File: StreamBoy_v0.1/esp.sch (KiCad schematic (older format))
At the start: 1 part

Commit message: Bunch of stuff
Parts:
- added C? (x3): C, Capacitor_SMD:C_0805_2012Metric, symbol Device:C
- added R?: R, Resistor_SMD:R_0805_2012Metric, symbol Device:R
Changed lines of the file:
@@
+	1    0    0    -1
+$EndComp
+$Comp
+L Device:R R?
+U 1 1 5E0D3F66
+P 2500 3200
+AR Path="/5E0FF68C/5E0D3F66" Ref="R?"  Part="1"
+AR Path="/5E0FBAC6/5E0D3F66" Ref="R?"  Part="1"
+F 0 "R?" H 2570 3246 50  0000 L CNN
+F 1 "R" H 2570 3155 50  0000 L CNN
+F 2 "Resistor_SMD:R_0805_2012Metric" V 2430 3200 50  0001 C CNN
+F 3 "~" H 2500 3200 50  0001 C CNN
+	1    2500 3200
+	1    0    0    -1
+$EndComp
+$Comp
+L Device:C C?
+U 1 1 5E0D4C34
+P 2550 2400
+F 0 "C?" H 2665 2446 50  0000 L CNN
+F 1 "C" H 2665 2355 50  0000 L CNN
+F 2 "Capacitor_SMD:C_0805_2012Metric" H 2588 2250 50  0001 C CNN
+F 3 "~" H 2550 2400 50  0001 C CNN
+	1    2550 2400
+	1    0    0    -1
+$EndComp
+$Comp
+L Device:C C?
+U 1 1 5E0D4F10
+P 2550 2800
+F 0 "C?" H 2665 2846 50  0000 L CNN
+F 1 "C" H 2665 2755 50  0000 L CNN
+F 2 "Capacitor_SMD:C_0805_2012Metric" H 2588 2650 50  0001 C CNN
+F 3 "~" H 2550 2800 50  0001 C CNN
+	1    2550 2800
+	1    0    0    -1
+$EndComp
+$Comp
+L Device:C C?
+U 1 1 5E0D4F16
+P 2900 2800
+F 0 "C?" H 3015 2846 50  0000 L CNN
+F 1 "C" H 3015 2755 50  0000 L CNN
+F 2 "Capacitor_SMD:C_0805_2012Metric" H 2938 2650 50  0001 C CNN
+F 3 "~" H 2900 2800 50  0001 C CNN
+	1    2900 2800
 	1    0    0    -1
 $EndComp

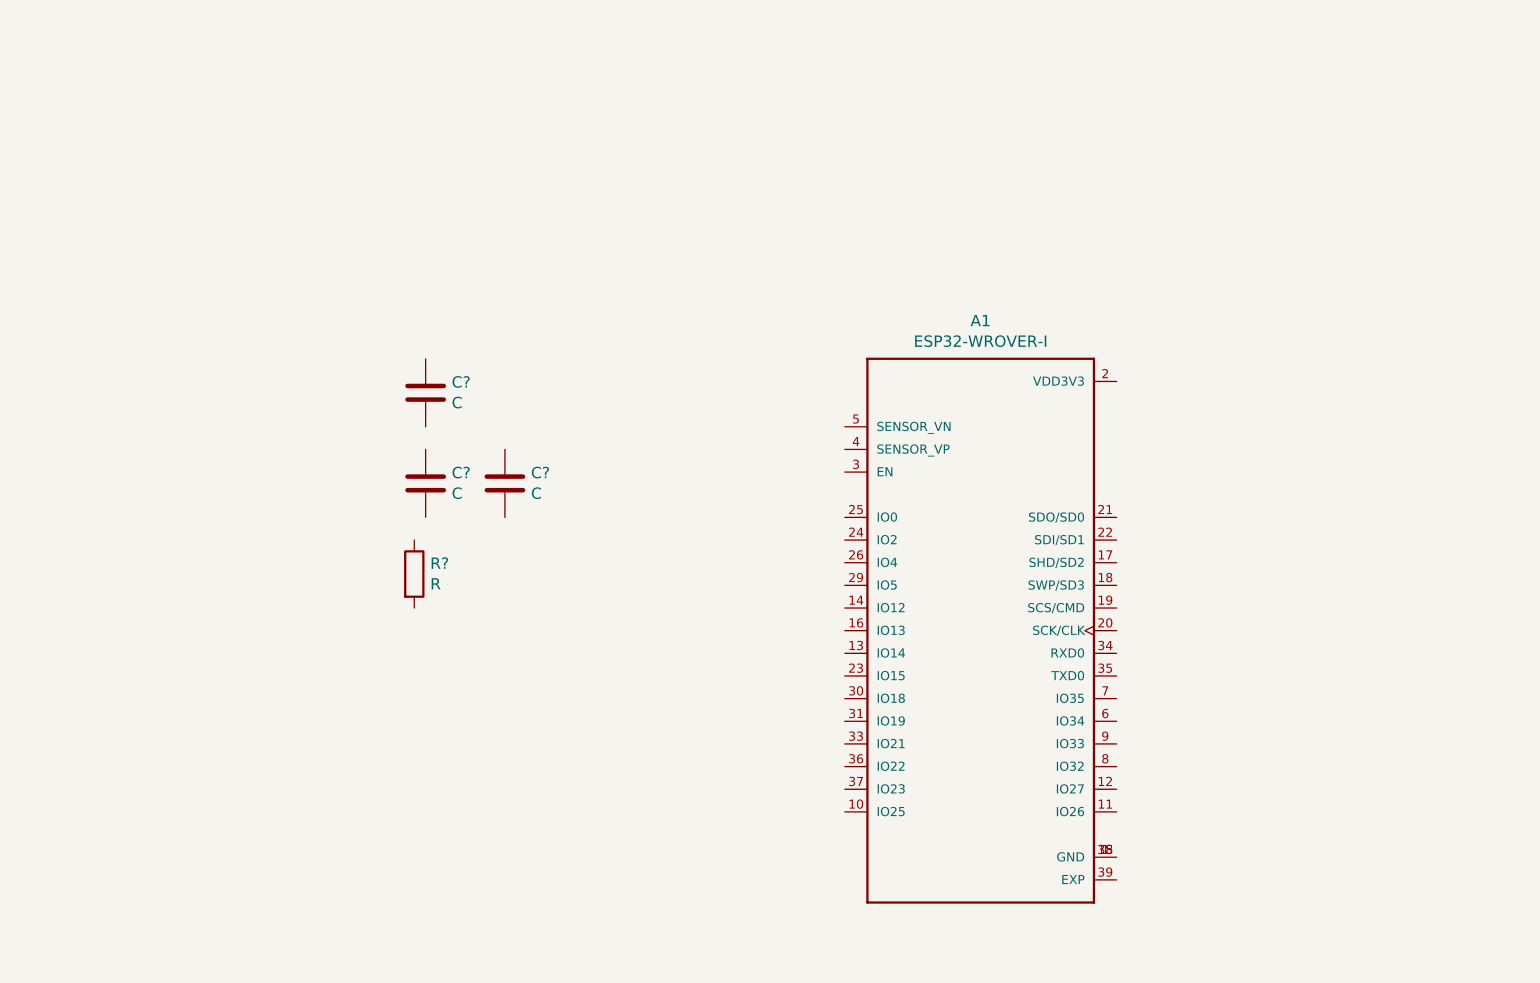
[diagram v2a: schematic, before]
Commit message: Add esp pins
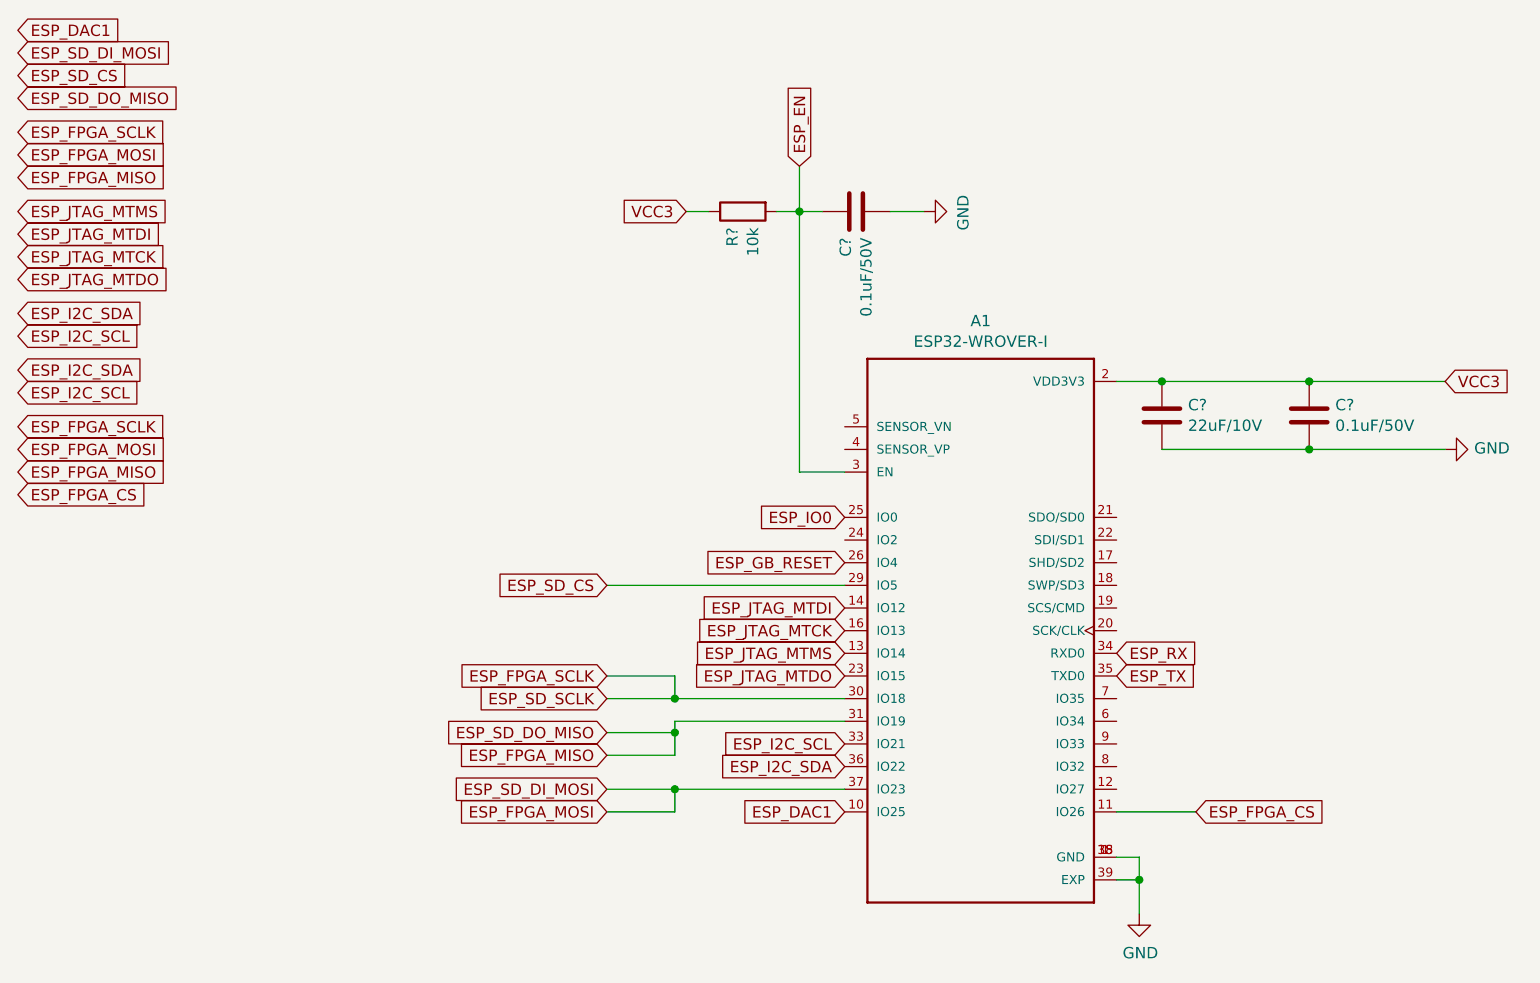
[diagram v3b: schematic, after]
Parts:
- removed C?: C, Capacitor_SMD:C_0805_2012Metric, symbol Device:C
- removed R?: R, Resistor_SMD:R_0805_2012Metric, symbol Device:R
- added C?: 0.1uF/50V, Capacitor_SMD:C_0805_2012Metric, symbol Device:C
- added R?: 10k, Resistor_SMD:R_0805_2012Metric, symbol Device:R
- C?: value C -> 22uF/10V
- C?: value C -> 0.1uF/50V
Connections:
- net VCC3: now reaches C?.1
- net VCC3: now also A1.2 (VDD3V3), C?.1, R?.1
- net GND: now reaches C?.2
- net GND: now also A1.1 (GND), A1.15 (GND), A1.38 (GND), A1.39 (EXP), C?.2, C?.2
- net ESP_DAC1: now reaches A1.10 (IO25)
- net ESP_FPGA_CS: now reaches A1.11 (IO26)
- net ESP_JTAG_MTMS: now reaches A1.13 (IO14)
- net ESP_JTAG_MTDI: now reaches A1.14 (IO12)
- net ESP_JTAG_MTCK: now reaches A1.16 (IO13)
- net ESP_JTAG_MTDO: now reaches A1.23 (IO15)
- net ESP_IO0: now reaches A1.25 (IO0)
- net ESP_GB_RESET: now reaches A1.26 (IO4)
- net ESP_SD_CS: now reaches A1.29 (IO5)
- net ESP_EN: now reaches A1.3 (EN)
- net ESP_EN: now also C?.1, R?.2
- net ESP_FPGA_SCLK: now reaches A1.30 (IO18)
- net ESP_FPGA_MISO: now reaches A1.31 (IO19)
- net ESP_I2C_SCL: now reaches A1.33 (IO21)
- net ESP_RX: now reaches A1.34 (RXD0)
- net ESP_TX: now reaches A1.35 (TXD0)
- net ESP_I2C_SDA: now reaches A1.36 (IO22)
- net ESP_FPGA_MOSI: now reaches A1.37 (IO23)
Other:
- moved on the sheet: C?

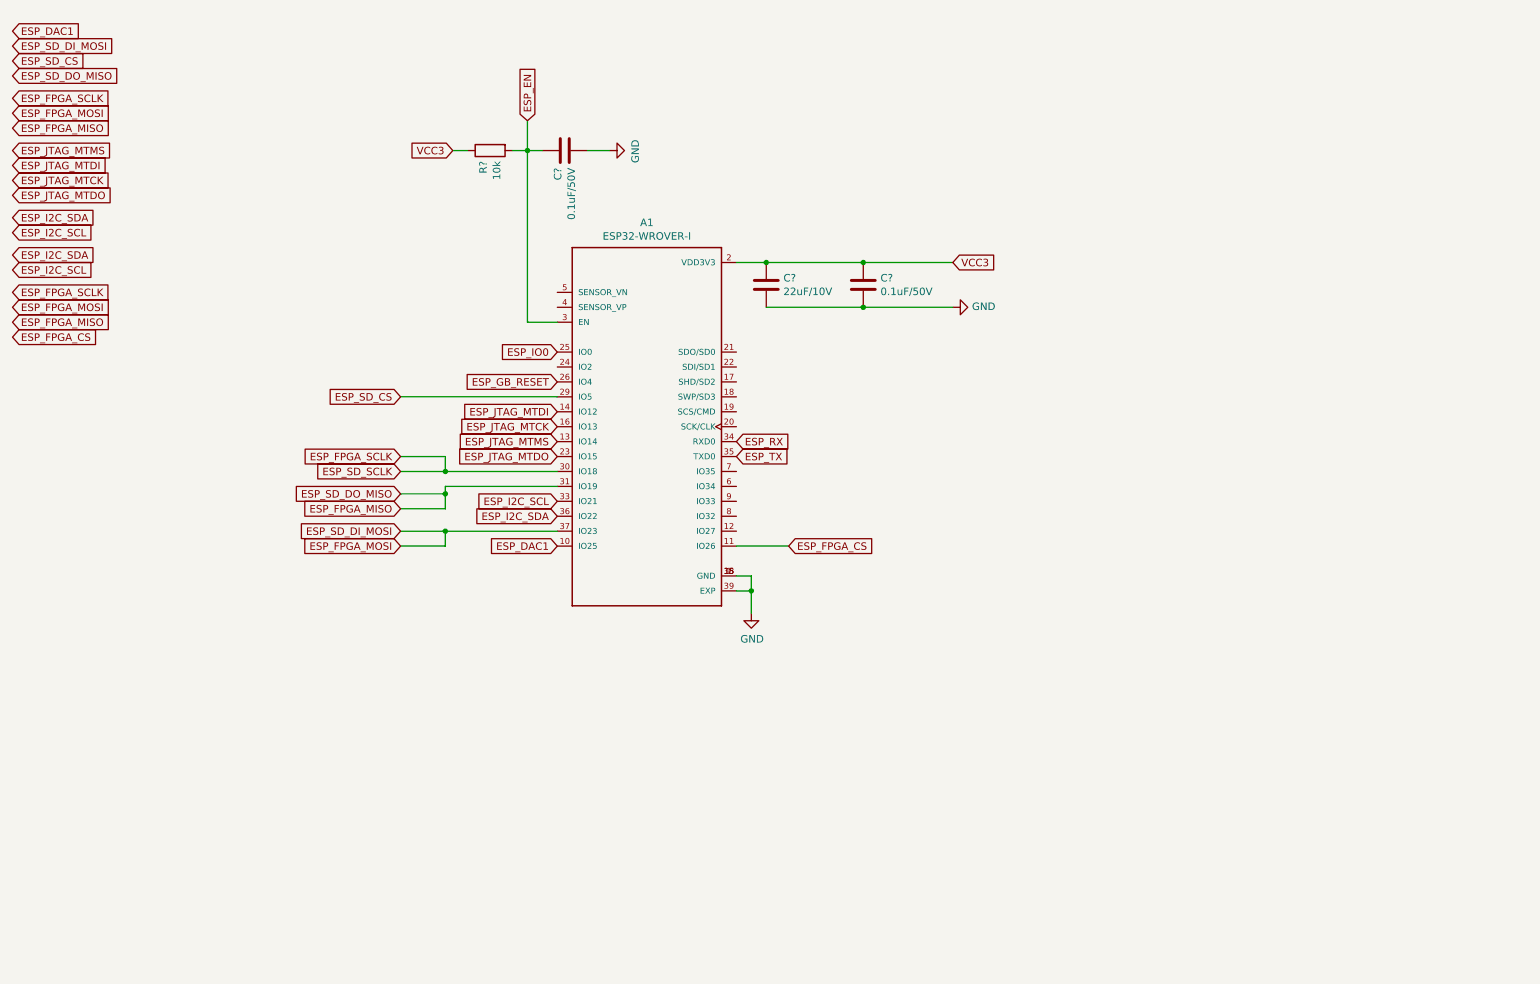
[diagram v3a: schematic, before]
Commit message: Flip RX/TX, Move esp prog. circuit
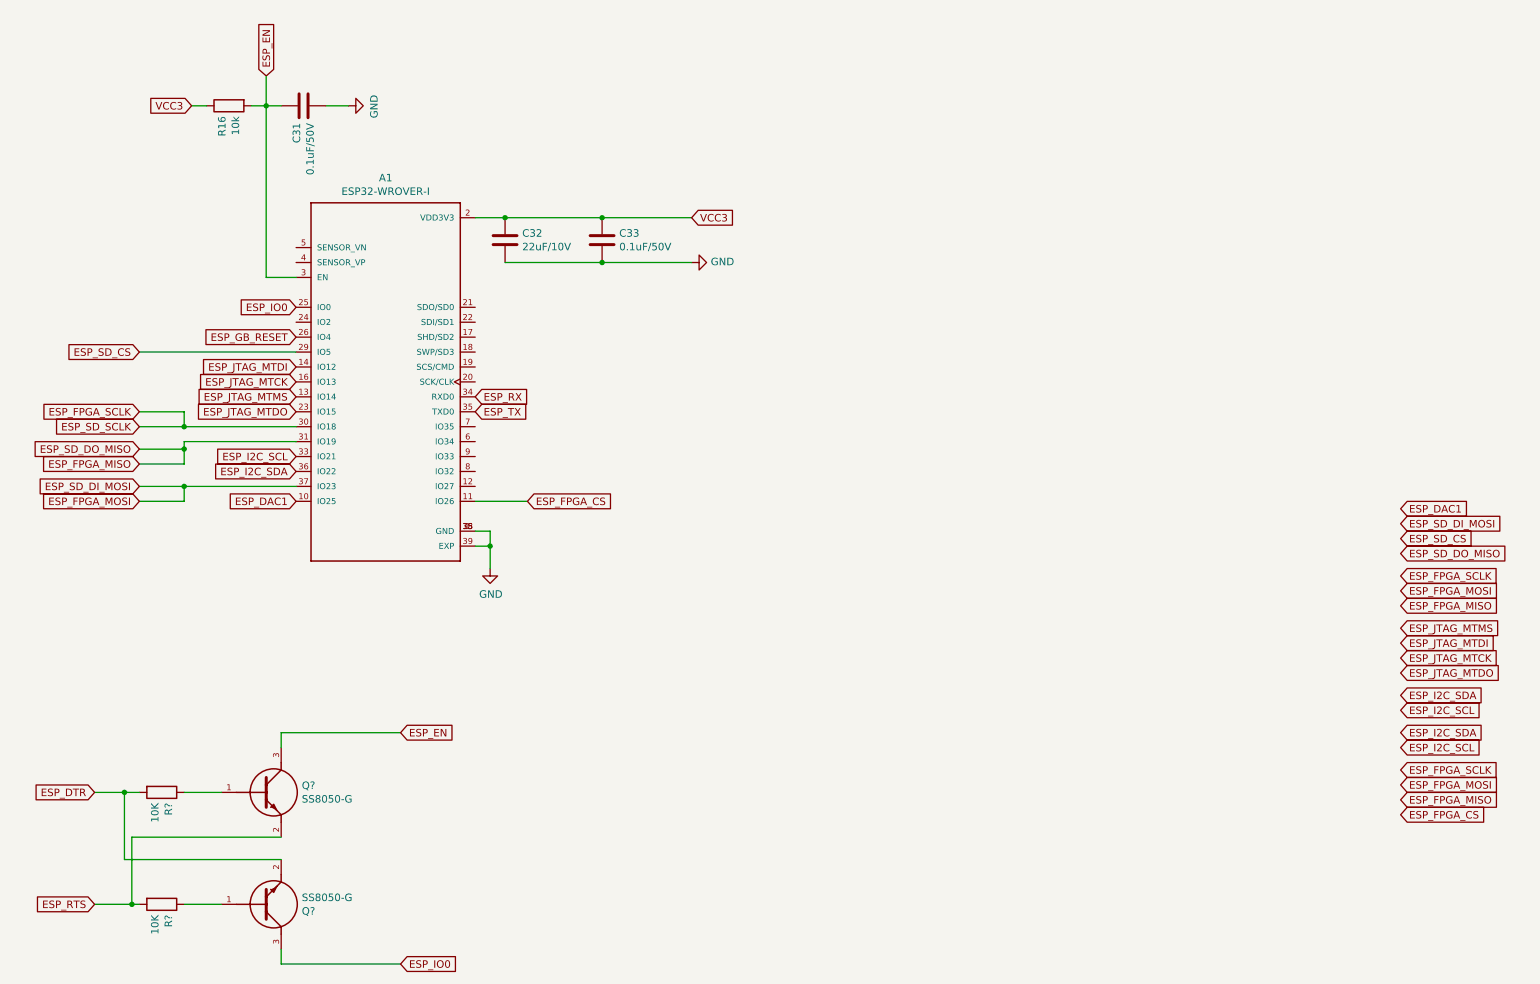
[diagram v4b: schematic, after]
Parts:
- added Q? (x2): SS8050-G, SOT95P240X115-3N, symbol SS8050-G:SS8050-G
- added R? (x2): 10K, Resistor_SMD:R_0805_2012Metric, symbol Device:R
- gave numbers to parts that had none: 4
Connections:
- net ESP_EN: now also Q?.3 (C)
- net ESP_IO0: now also Q?.3 (C)
- new net: Q?.1 (B), R?.1 (x2)
- new net ESP_DTR: Q?.2 (E), R?.2
- new net ESP_RTS: Q?.2 (E), R?.2
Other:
- moved on the sheet: A1, C31, C32, C33, R16

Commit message: Update some labels
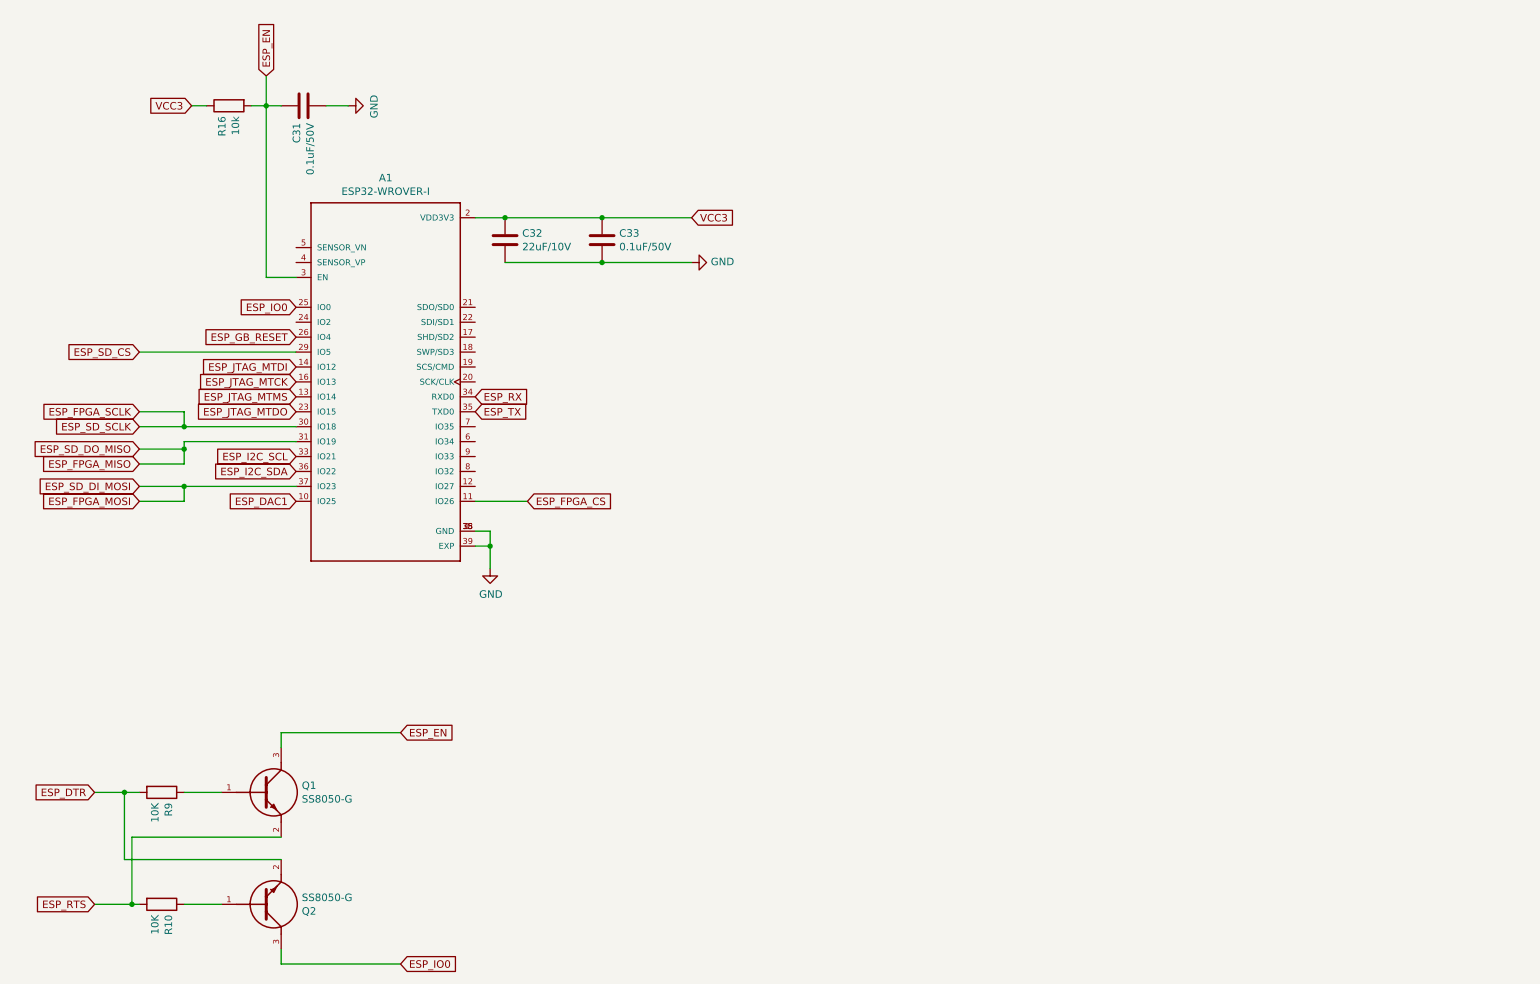
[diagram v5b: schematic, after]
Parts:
- gave numbers to parts that had none: 4
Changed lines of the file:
@@
 	1    0    0    -1
 $EndComp
-Text GLabel 10050 4800 2    50   Input ~ 0
-ESP_JTAG_MTMS
-Text GLabel 10050 4900 2    50   Input ~ 0
-ESP_JTAG_MTDI
-Text GLabel 10050 5000 2    50   Input ~ 0
-ESP_JTAG_MTCK
-Text GLabel 10050 5100 2    50   Input ~ 0
-ESP_JTAG_MTDO
 Text GLabel 2650 3350 0    50   Input ~ 0
 ESP_JTAG_MTDO
@@
 Text GLabel 2650 3950 0    50   Input ~ 0
 ESP_DAC1
-Text GLabel 10050 5500 2    50   Input ~ 0
-ESP_I2C_SDA
-Text GLabel 10050 5600 2    50   Input ~ 0
-ESP_I2C_SCL
 Text GLabel 1600 2950 0    50   Input ~ 0
 ESP_SD_CS
@@
 Text GLabel 1600 3600 0    50   Input ~ 0
 ESP_SD_DO_MISO
-Text GLabel 10050 4200 2    50   Input ~ 0
-ESP_SD_CS
-Text GLabel 10050 4000 2    50   Input ~ 0
-ESP_DAC1
-Text GLabel 10050 4100 2    50   Input ~ 0
-ESP_SD_DI_MOSI
-Text GLabel 10050 4300 2    50   Input ~ 0
-ESP_SD_DO_MISO
-Text GLabel 10050 5250 2    50   Input ~ 0
-ESP_I2C_SDA
-Text GLabel 10050 5350 2    50   Input ~ 0
-ESP_I2C_SCL
-Text GLabel 10050 5750 2    50   Input ~ 0
-ESP_FPGA_SCLK
-Text GLabel 10050 5850 2    50   Input ~ 0
-ESP_FPGA_MOSI
-Text GLabel 10050 5950 2    50   Input ~ 0
-ESP_FPGA_MISO
-Text GLabel 10050 4450 2    50   Input ~ 0
-ESP_FPGA_SCLK
-Text GLabel 10050 4550 2    50   Input ~ 0
-ESP_FPGA_MOSI
-Text GLabel 10050 4650 2    50   Input ~ 0
-ESP_FPGA_MISO
-Text GLabel 10050 6050 2    50   Input ~ 0
-ESP_FPGA_CS
 Text GLabel 4200 3950 2    50   Input ~ 0
 ESP_FPGA_CS
@@
 AR Path="/5E0FF68C/5E15CB2A" Ref="R?"  Part="1"
 AR Path="/5E07E0B7/5E15CB2A" Ref="R?"  Part="1"
-F 0 "R?" H 1820 5946 50  0000 L CNN
+AR Path="/5E0FBAC6/5E15CB2A" Ref="R9"  Part="1"
+F 0 "R9" H 1820 5946 50  0000 L CNN
 F 1 "10K" H 1820 5855 50  0000 L CNN
 F 2 "Resistor_SMD:R_0805_2012Metric" V 1680 5900 50  0001 C CNN
@@
 AR Path="/5E0FF68C/5E15CB30" Ref="R?"  Part="1"
 AR Path="/5E07E0B7/5E15CB30" Ref="R?"  Part="1"
-F 0 "R?" H 1820 6696 50  0000 L CNN
+AR Path="/5E0FBAC6/5E15CB30" Ref="R10"  Part="1"
+F 0 "R10" H 1820 6696 50  0000 L CNN
 F 1 "10K" H 1820 6605 50  0000 L CNN
 F 2 "Resistor_SMD:R_0805_2012Metric" V 1680 6650 50  0001 C CNN
@@
 U 1 1 5E15CB3B
 P 2150 5900
-F 0 "Q?" H 2688 5946 50  0000 L CNN
+AR Path="/5E07E0B7/5E15CB3B" Ref="Q?"  Part="1"
+AR Path="/5E0FBAC6/5E15CB3B" Ref="Q1"  Part="1"
+F 0 "Q1" H 2688 5946 50  0000 L CNN
 F 1 "SS8050-G" H 2688 5855 50  0000 L CNN
 F 2 "SOT95P240X115-3N" H 2150 5900 50  0001 L BNN
@@
 U 1 1 5E15CB46
 P 2150 6650
-F 0 "Q?" H 2688 6696 50  0000 L CNN
+AR Path="/5E07E0B7/5E15CB46" Ref="Q?"  Part="1"
+AR Path="/5E0FBAC6/5E15CB46" Ref="Q2"  Part="1"
+F 0 "Q2" H 2688 6696 50  0000 L CNN
 F 1 "SS8050-G" H 2688 6605 50  0000 L CNN
 F 2 "SOT95P240X115-3N" H 2150 6650 50  0001 L BNN
